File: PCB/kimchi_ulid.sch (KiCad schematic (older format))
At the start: 32 parts, among them J1 DF40HC(3.5)-60DS, J2 DF40HC(3.5)-60DS, J3 1-292303-6, J4 54-00177, J5 RCJ-2123, J6 RCJ-2123, U1 24C32, U2 SN74LV1T34DBVRG4, U3 SGTL5000XNLA3, X1 ASFL1-12.288MHZ-EC-T

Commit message: redesigned circuit around WM8750 codec, added needed components to library
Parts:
- removed C5: C0402C104K9PACTU, kimchi_ulid:C0402, symbol kimchi_ulid:C0402C104K9PACTU
- removed C7: T491A105K010AT, kimchi_ulid:C1206, symbol kimchi_ulid:T491A105K010AT
- removed J3: 1-292303-6, kimchi_ulid:TE_1-292303-6, symbol kimchi_ulid:1-292303-6
- removed U3: SGTL5000XNLA3, kimchi_ulid:QFN40P300X300X60-21N, symbol kimchi_ulid:SGTL5000XNLA3
- added C13, C5: T491D227M010AT, kimchi_ulid:T491D227M010AT, symbol kimchi_ulid:T491D227M010AT
- added C14, C15: T494A106M006AT, kimchi_ulid:T494A106M006AT, symbol kimchi_ulid:T494A106M006AT
- added C16, C17, C7: C0402C104K9PACTU, kimchi_ulid:C0402, symbol kimchi_ulid:C0402C104K9PACTU
- added FB5: FBMJ1608HM180NTR, kimchi_ulid:R0603, symbol kimchi_ulid:FBMJ1608HM180NTR
- added R2: RC0603FR-0747KL, AVR-KiCAD-Lib-Resistors:R0603, symbol AVR-KiCAD-Lib-Resistors:RC0603FR-0747KL
- added U3: WM8750CJLGEFL, kimchi_ulid:QFN-32_EP_5x5_Pitch0.5mm, symbol kimchi_ulid:WM8750CJLGEFL
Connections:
- net labels added: I2S_CSB, I2S_SCLK, I2S_SDIN, MCLK
- net labels removed: HPOUT_L, HPOUT_R
- wire segments 128 -> 138
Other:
- note added: "Audio Codec"
- note added: "Codec Master Clock"
- note added: "Headset (Phones/Mic)"
- note added: "Stereo In (RCA)"
- note added: "Stereo Out (RCA)"
- moved on the sheet: C1, C10, C11, C12, C2, C6, C8, C9, FB1, FB2, FB3, FB4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

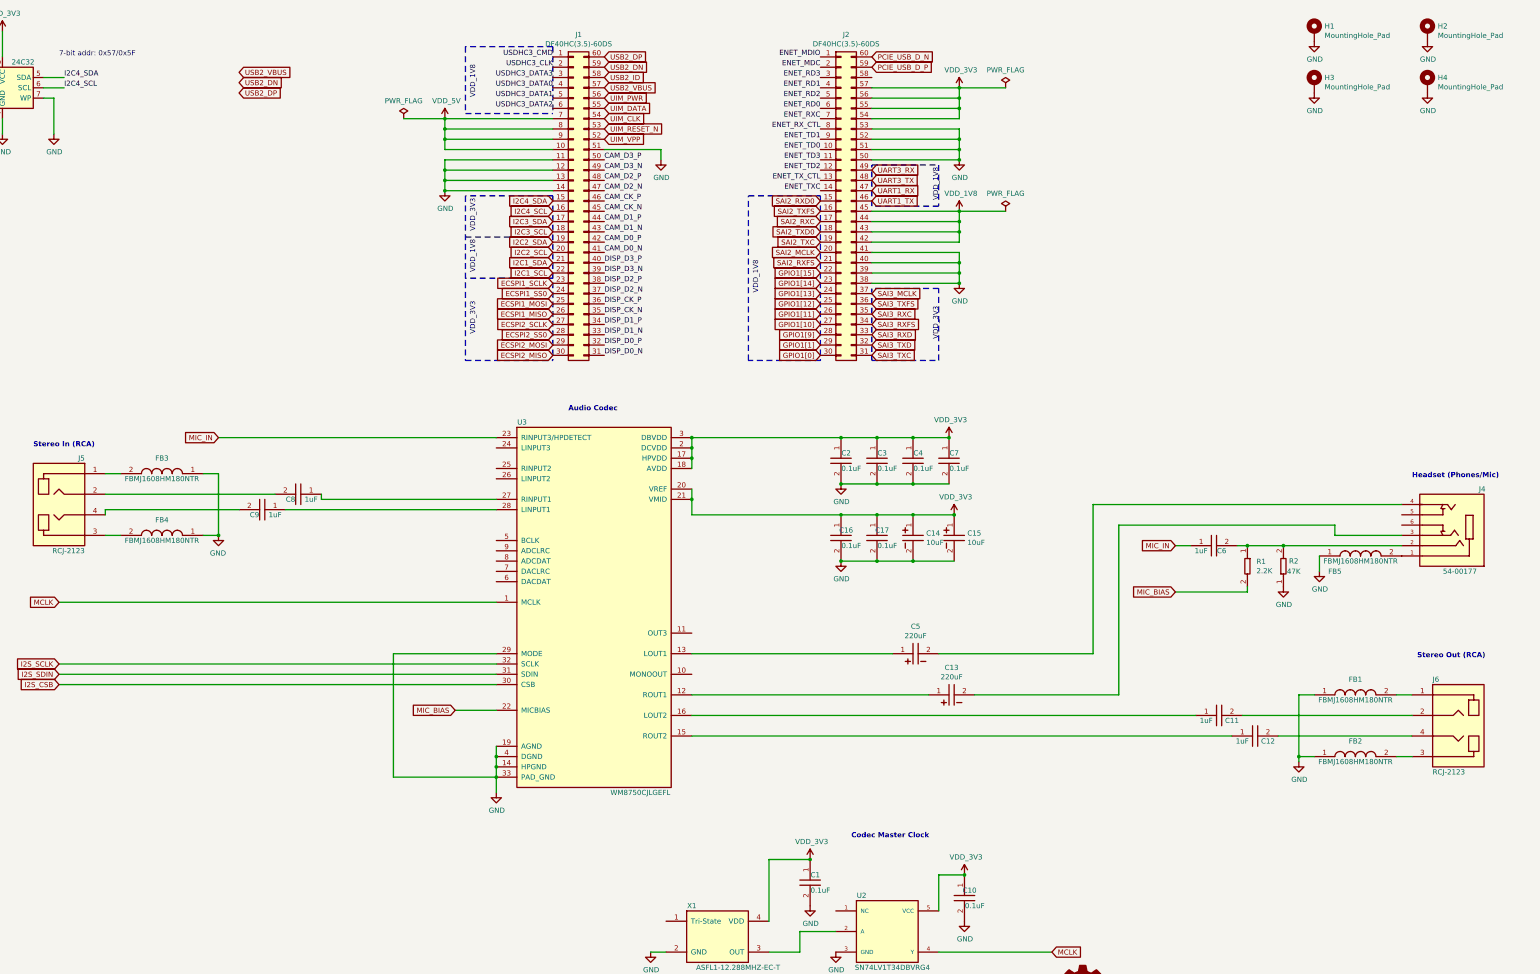
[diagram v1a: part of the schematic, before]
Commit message: Route In Progress
Now doing the intial route of the board, still very much a work in progress, have the pwoer planes figured out and general component placenment. All components now have 3D models.
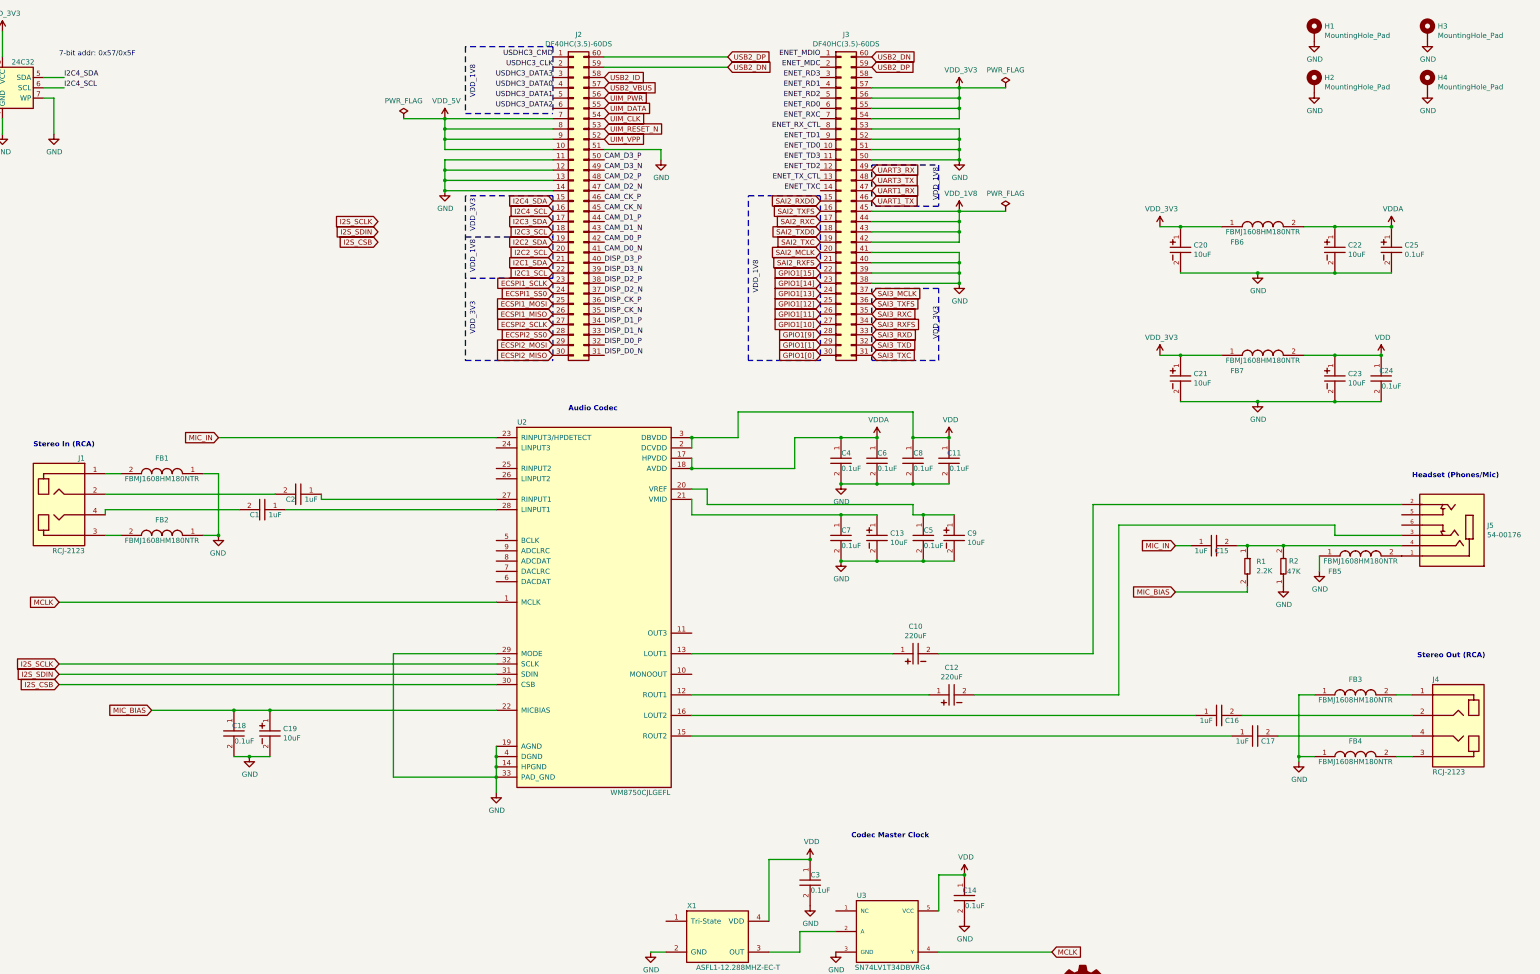
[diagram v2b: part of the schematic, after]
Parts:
- removed J4: 54-00177, kimchi_ulid:54-00177, symbol kimchi_ulid:54-00177
- added C18, C24: C0402C104K9PACTU, kimchi_ulid:C0402, symbol kimchi_ulid:C0402C104K9PACTU
- added C19, C20, C21, C22, C23: T494A106M006AT, kimchi_ulid:T494A106M006AT, symbol kimchi_ulid:T494A106M006AT
- added C25: UZP1H0R1MCL1GB, kimchi_ulid:UZP1H0R1MCL1GB, symbol kimchi_ulid:UZP1H0R1MCL1GB
- added FB6, FB7: FBMJ1608HM180NTR, kimchi_ulid:R0603, symbol kimchi_ulid:FBMJ1608HM180NTR
- added J5: 54-00176, kimchi_ulid:54-00176, symbol kimchi_ulid:54-00176
- renumbered C9 to C1, C5 to C10, C7 to C11, C13 to C12, C15 to C13, C10 to C14, C6 to C15, C11 to C16, C12 to C17, C8 to C2, C1 to C3, C2 to C4, C16 to C5, C3 to C6, C17 to C7, C4 to C8, C14 to C9, FB3 to FB1, FB4 to FB2, FB1 to FB3, FB2 to FB4, H3 to H2, H2 to H3, J5 to J1, J1 to J2, J2 to J3, J6 to J4, U3 to U2, U2 to U3
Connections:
- net PCIE_USB_D_N is gone; now on net USB2_DN: J3.60 (Pin_60)
- net PCIE_USB_D_P is gone; now on net USB2_DP: J3.59 (Pin_59)
- net GND: now also C18.2, C19.2, C20.2, C21.2, C22.2, C23.2, C24.2, C25.2
- net MIC_BIAS: now also C18.1, C19.1
- net VDD_3V3: now also C20.1, C21.1, FB6.1, FB7.1; no longer C11.1, C13.1, C14.1, C3.1, C4.1, C5.1, C6.1, C7.1, C8.1, C9.1, U2.17 (HPVDD), U2.18 (AVDD), U2.2 (DCVDD), U2.20 (VREF), U2.21 (VMID), U2.3 (DBVDD), U3.5 (VCC), X1.4 (VDD)
- net at C15.2, R1.1, R2.2: now also J5.4
- net at FB5.2: now also J5.1
- net at C12.2: now also J5.3
- net at C10.2: now also J5.2
- new net: C5.1, C9.1, U2.20 (VREF)
- new net: C13.1, C7.1, U2.21 (VMID)
- new net VDD: C11.1, C14.1, C23.1, C24.1, C3.1, C8.1, FB7.2, U2.2 (DCVDD), U2.3 (DBVDD), U3.5 (VCC), X1.4 (VDD)
- new net VDDA: C22.1, C25.1, C4.1, C6.1, FB6.2, U2.17 (HPVDD), U2.18 (AVDD)
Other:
- moved on the sheet: C13, C5, C7, C9

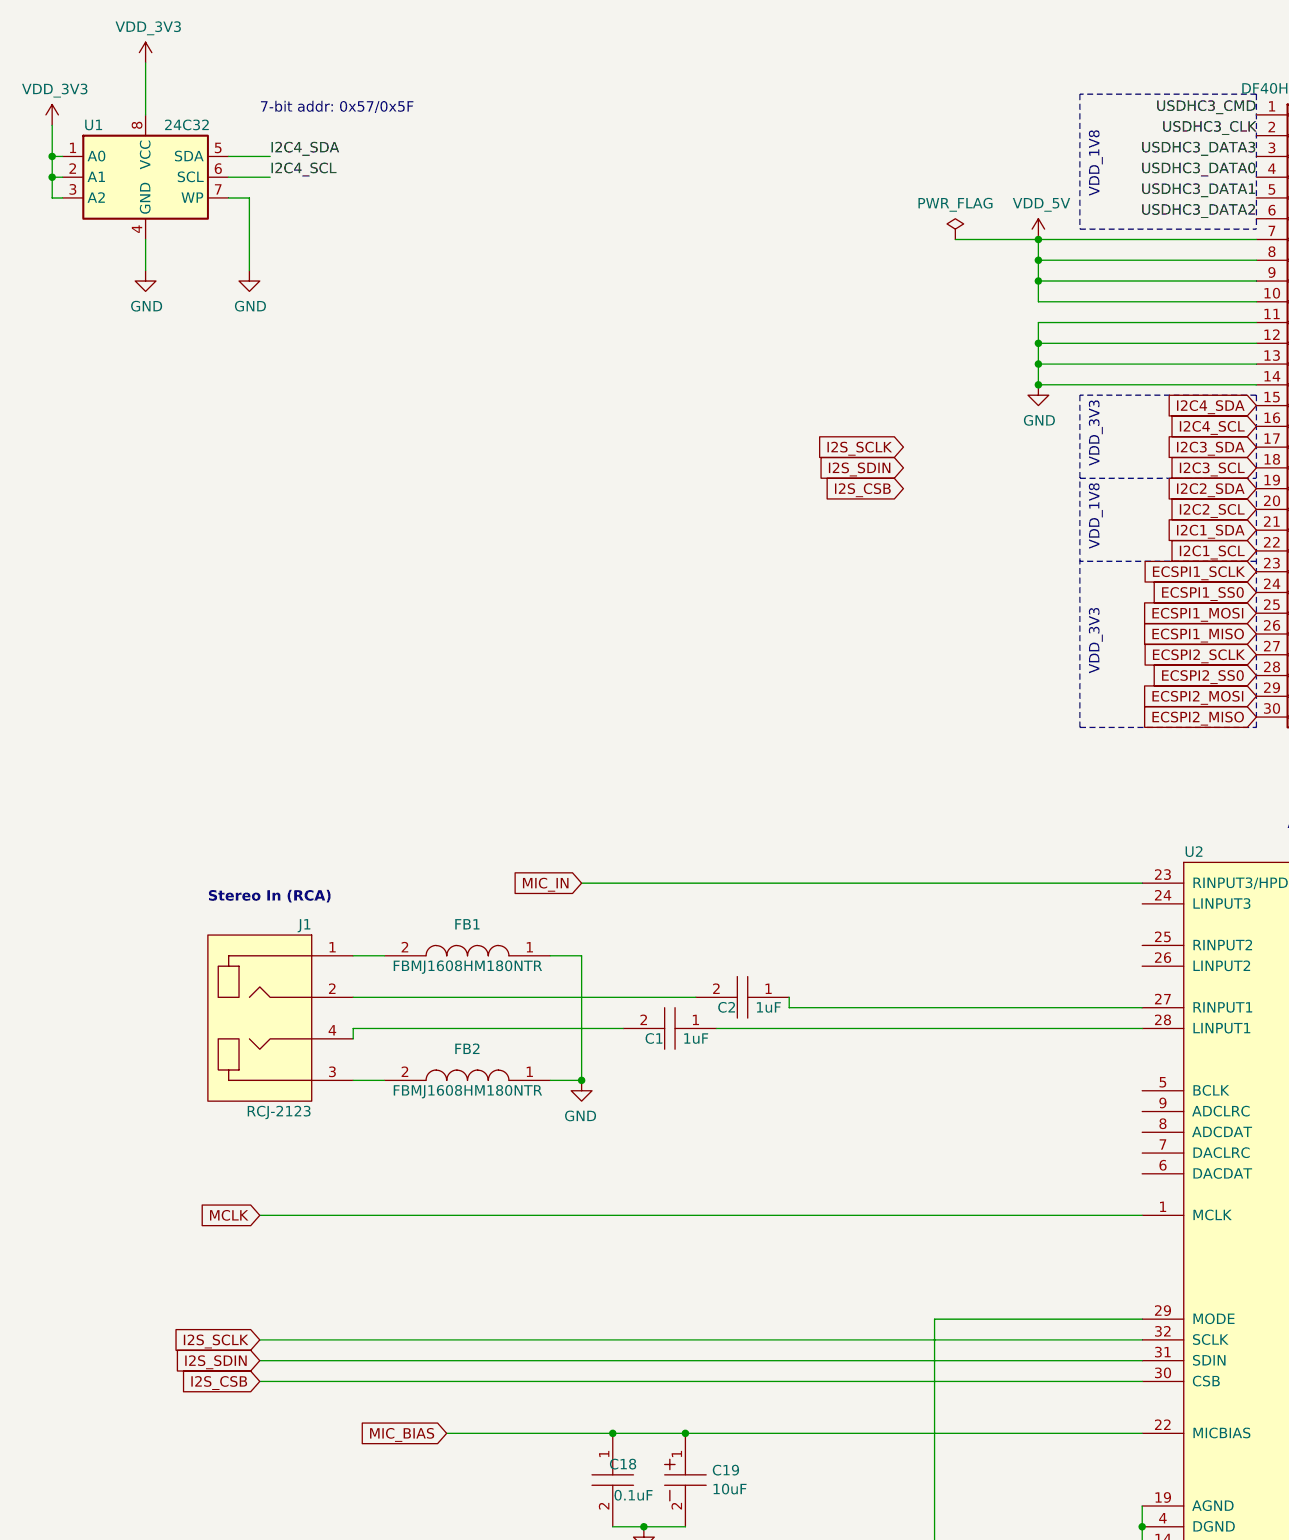
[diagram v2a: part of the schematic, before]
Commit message: First Route Pass Completed
Completed first pass of routting the board. Need to adjust trace width for analog front ends for audio in and out.
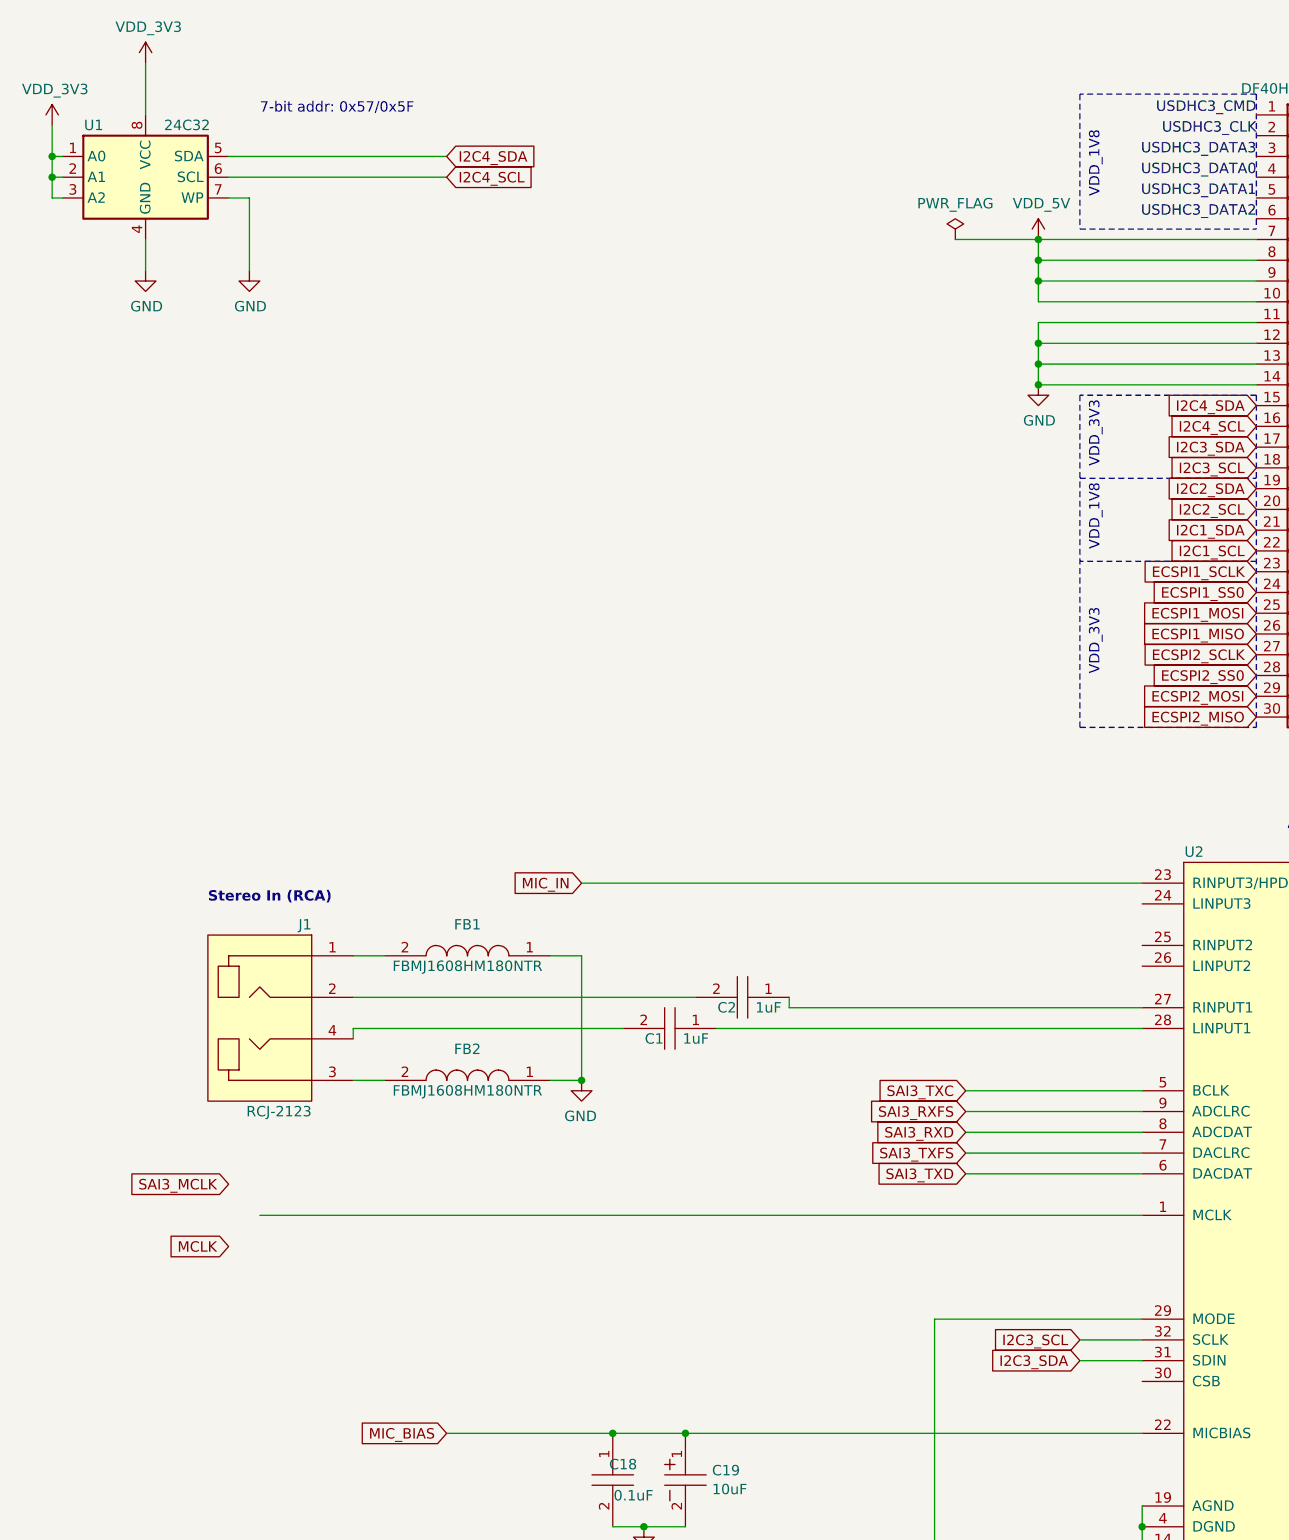
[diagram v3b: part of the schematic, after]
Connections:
- net I2S_SCLK is gone; now on net I2C3_SCL: U2.32 (SCLK)
- net I2S_SDIN is gone; now on net I2C3_SDA: U2.31 (SDIN)
- net MCLK: no longer U2.1 (MCLK)
- net SAI3_RXD: now also U2.8 (ADCDAT)
- net SAI3_RXFS: now also U2.9 (ADCLRC)
- net SAI3_TXC: now also U2.5 (BCLK)
- net SAI3_TXD: now also U2.6 (DACDAT)
- net SAI3_TXFS: now also U2.7 (DACLRC)
- net I2S_CSB: no longer names the net of U2.30 (CSB)
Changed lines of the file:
@@
 	2000 1650 2000 2000
 Wire Wire Line
-	2100 1550 1900 1550
-Wire Wire Line
-	2100 1450 1900 1450
+	2950 1550 1900 1550
+Wire Wire Line
+	2950 1450 1900 1450
 $Comp
 L kimchi_ulid-rescue:24LC16-Memory_EEPROM U1
@@
 	1    0    0    -1
 $EndComp
-Text Label 2100 1550 0    50   ~ 0
-I2C4_SCL
-Text Label 2100 1450 0    50   ~ 0
-I2C4_SDA
 Text Notes 2050 1250 0    50   ~ 0
 7-bit addr: 0x57/0x5F
@@
 Wire Wire Line
 	5300 8250 6300 8250
-Wire Wire Line
-	6300 7150 2050 7150
-Wire Wire Line
-	6300 7250 2050 7250
-Wire Wire Line
-	6300 7350 2050 7350
 $Comp
 L kimchi_ulid:T491D227M010AT C10
@@
 	1    0    0    -1
 $EndComp
-Text GLabel 2050 6550 0    50   Input ~ 0
+Text GLabel 1900 6700 0    50   Input ~ 0
 MCLK
 Wire Wire Line
@@
 Text Notes 1800 5050 0    50   ~ 10
 Stereo In (RCA)
-Text GLabel 2050 7150 0    50   Input ~ 0
-I2S_SCLK
-Text GLabel 2050 7350 0    50   Input ~ 0
-I2S_CSB
-Text GLabel 2050 7250 0    50   Input ~ 0
-I2S_SDIN
 Text Notes 9750 8850 0    50   ~ 10
 Codec Master Clock
@@
 Wire Wire Line
 	7350 1350 8550 1350
-Text GLabel 5150 2850 0    50   Input ~ 0
-I2S_SCLK
-Text GLabel 5150 3050 0    50   Input ~ 0
-I2S_CSB
-Text GLabel 5150 2950 0    50   Input ~ 0
-I2S_SDIN
 $Comp
 L kimchi_ulid:FBMJ1608HM180NTR FB6
@@
 Wire Wire Line
 	10000 6150 10450 6150
+Text GLabel 2950 1450 2    50   Input ~ 0
+I2C4_SDA
+Text GLabel 2950 1550 2    50   Input ~ 0
+I2C4_SCL
+Text GLabel 1900 6400 0    50   Input ~ 0
+SAI3_MCLK
+Text GLabel 5450 5950 0    50   Input ~ 0
+SAI3_TXC
+Text GLabel 5450 6250 0    50   Input ~ 0
+SAI3_TXFS
+Text GLabel 5450 6150 0    50   Input ~ 0
+SAI3_RXD
+Text GLabel 5450 6050 0    50   Input ~ 0
+SAI3_RXFS
+Text GLabel 5450 6350 0    50   Input ~ 0
+SAI3_TXD
+Wire Wire Line
+	6300 5950 5450 5950
+Wire Wire Line
+	5450 6050 6300 6050
+Wire Wire Line
+	6300 6150 5450 6150
+Wire Wire Line
+	5450 6250 6300 6250
+Wire Wire Line
+	6300 6350 5450 6350
+Text GLabel 6000 7250 0    50   Input ~ 0
+I2C3_SDA
+Text GLabel 6000 7150 0    50   Input ~ 0
+I2C3_SCL
+Wire Wire Line
+	6000 7150 6300 7150
+Wire Wire Line
+	6300 7250 6000 7250
 $EndSCHEMATC

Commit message: MCLK Jumper
MCLK jumper added, trace width tweaked and DRC passed.
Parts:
- added J6: Conn_01x03_Male, Pin_Headers:Pin_Header_Straight_1x03_Pitch2.54mm, symbol Connector:Conn_01x03_Male
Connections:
- net MCLK: now also J6.3 (Pin_3)
- net SAI3_MCLK: now also J6.1 (Pin_1)
- net at U2.1 (MCLK): now also J6.2 (Pin_2)
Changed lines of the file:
@@
 	1    0    0    -1
 $EndComp
-Text GLabel 1900 6700 0    50   Input ~ 0
+Text GLabel 2050 6650 2    50   Input ~ 0
 MCLK
 Wire Wire Line
@@
 Text GLabel 2950 1550 2    50   Input ~ 0
 I2C4_SCL
-Text GLabel 1900 6400 0    50   Input ~ 0
+Text GLabel 2050 6450 2    50   Input ~ 0
 SAI3_MCLK
 Text GLabel 5450 5950 0    50   Input ~ 0
@@
 Wire Wire Line
 	6300 7250 6000 7250
+$Comp
+L Connector:Conn_01x03_Male J6
+U 1 1 5FE51E54
+P 1850 6550
+F 0 "J6" H 1800 6750 50  0000 C CNN
+F 1 "Conn_01x03_Male" H 1850 6350 50  0000 C CNN
+F 2 "Pin_Headers:Pin_Header_Straight_1x03_Pitch2.54mm" H 1850 6550 50  0001 C CNN
+F 3 "~" H 1850 6550 50  0001 C CNN
+	1    1850 6550
+	1    0    0    -1
+$EndComp
 $EndSCHEMATC

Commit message: Fab FIles
Fab files generated
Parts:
- added L1: GG_LOGO, kimchi_ulid:groupgets_logo, symbol kimchi_ulid:GG_LOGO
- added L2: OSHPARK_LOGO, kimchi_ulid:oshpark_logo, symbol kimchi_ulid:OSHPARK_LOGO
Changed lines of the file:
@@
+	1    0    0    -1
+$EndComp
+$Comp
+L kimchi_ulid:GG_LOGO L1
+U 1 1 6012EC1D
+P 4300 9200
+F 0 "L1" H 4350 9245 50  0000 L CNN
+F 1 "GG_LOGO" H 4350 9154 50  0000 L CNN
+F 2 "kimchi_ulid:groupgets_logo" H 4300 9200 50  0001 C CNN
+F 3 "" H 4300 9200 50  0001 C CNN
+	1    4300 9200
+	1    0    0    -1
+$EndComp
+$Comp
+L kimchi_ulid:OSHPARK_LOGO L2
+U 1 1 6013219F
+P 4300 9400
+F 0 "L2" H 4350 9445 50  0000 L CNN
+F 1 "OSHPARK_LOGO" H 4350 9354 50  0000 L CNN
+F 2 "kimchi_ulid:oshpark_logo" H 4300 9400 50  0001 C CNN
+F 3 "" H 4300 9400 50  0001 C CNN
+	1    4300 9400
 	1    0    0    -1
 $EndComp
